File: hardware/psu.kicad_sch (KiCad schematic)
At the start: 14 parts, among them Q501 MMBT5551, U501 MAX15062AATA+T

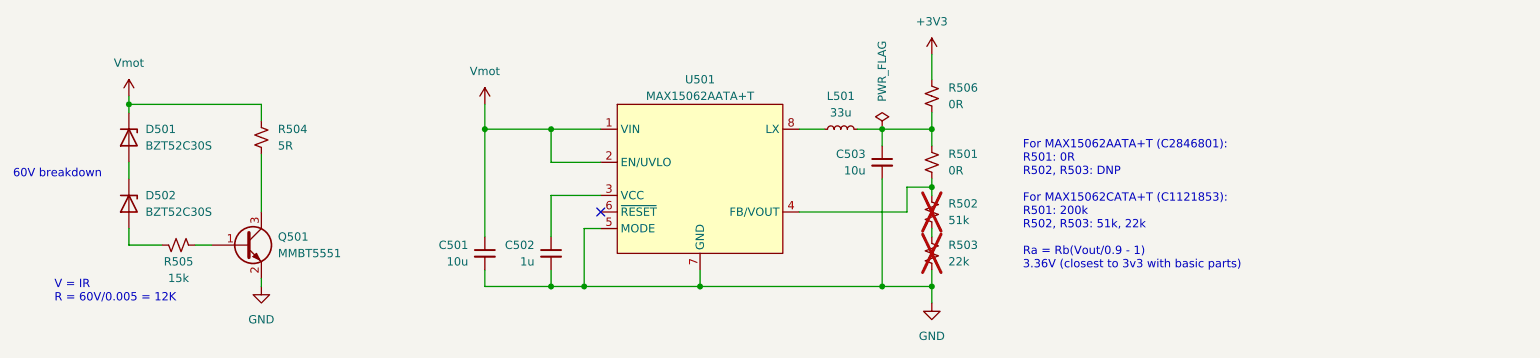
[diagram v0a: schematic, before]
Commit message: fix erc failures
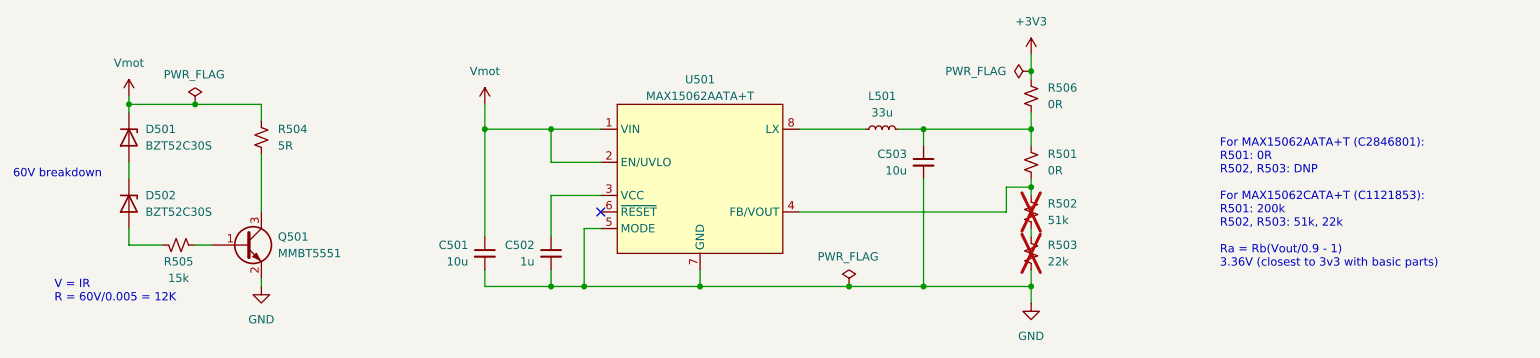
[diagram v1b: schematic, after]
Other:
- moved on the sheet: C503, L501, R501, R502, R503, R506

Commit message: Update BOM field LCSC ID
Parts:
- C501, C503: LCSC ID (none) -> C440198; LCSC Part C440198 -> (none)
- C502: LCSC ID (none) -> C52923; LCSC Part C52923 -> (none)
- D501, D502: LCSC ID (none) -> C22622; LCSC Part C22622 -> (none)
- L501: LCSC ID (none) -> C602034; LCSC Part C602034 -> (none)
- Q501: LCSC ID (none) -> C2145; LCSC Part C2145 -> (none)
- R501: LCSC ID (none) -> C17168; LCSC Part C17168 -> (none)
- R502: LCSC ID (none) -> C25794; LCSC Part C25794 -> (none)
- R503: LCSC ID (none) -> C25768; LCSC Part C25768 -> (none)
- R504: LCSC ID (none) -> C22936; LCSC Part C22936 -> (none)
- R505: LCSC ID (none) -> C25756; LCSC Part C25756 -> (none)
- R506: LCSC ID (none) -> C21189; LCSC Part C21189 -> (none)
- U501: LCSC ID (none) -> C2846801; LCSC Part C2846801 -> (none)
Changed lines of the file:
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@@
 			)
 		)
-		(property "LCSC Part" "C2145"
+		(property "LCSC ID" "C2145"
 			(at 76.2 92.71 0)
 			(effects
@@
 			)
 		)
-		(property "LCSC Part" "C52923"
+		(property "LCSC ID" "C52923"
 			(at 123.19 93.98 0)
 			(effects
@@
 			)
 		)
-		(property "LCSC Part" "C25756"
+		(property "LCSC ID" "C25756"
 			(at 66.04 92.71 0)
 			(effects
@@
 			)
 		)
-		(property "LCSC Part" "C2846801"
-			(at 146.05 101.6 0)
+		(property "LCSC ID" "C2846801"
+			(at 146.05 87.63 0)
 			(effects
 				(font
@@
 			)
 		)
-		(property "LCSC Part" "C22622"
+		(property "LCSC ID" "C22622"
 			(at 58.42 86.36 0)
 			(effects
@@
 			)
 		)
-		(property "LCSC Part" "C25768"
+		(property "LCSC ID" "C25768"
 			(at 196.85 93.98 0)
 			(effects
@@
 			)
 		)
-		(property "LCSC Part" "C22622"
+		(property "LCSC ID" "C22622"
 			(at 58.42 76.2 0)
 			(effects
@@
 			)
 		)
-		(property "LCSC Part" "C22936"
+		(property "LCSC ID" "C22936"
 			(at 78.74 76.2 0)
 			(effects
@@
 			)
 		)
-		(property "LCSC Part" "C21189"
+		(property "LCSC ID" "C21189"
 			(at 196.85 69.85 0)
 			(effects
@@
 			)
 		)
-		(property "LCSC Part" "C602034"
+		(property "LCSC ID" "C602034"
 			(at 173.99 74.93 0)
 			(effects
@@
 			)
 		)
-		(property "LCSC Part" "C440198"
+		(property "LCSC ID" "C440198"
 			(at 113.03 93.98 0)
 			(effects
@@
 			)
 		)
-		(property "LCSC Part" "C25794"
+		(property "LCSC ID" "C25794"
 			(at 196.85 87.63 0)
 			(effects
@@
 			)
 		)
-		(property "LCSC Part" "C440198"
+		(property "LCSC ID" "C440198"
 			(at 180.34 80.01 0)
 			(effects
@@
 			)
 		)
-		(property "LCSC Part" "C17168"
+		(property "LCSC ID" "C17168"
 			(at 196.85 80.01 0)
 			(effects

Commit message: fix BOM to use basic parts again
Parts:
- D501, D502: LCSC ID C22622 -> C19077418
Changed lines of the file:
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@@
 			)
 		)
-		(property "LCSC ID" "C22622"
+		(property "LCSC ID" "C19077418"
 			(at 58.42 86.36 0)
 			(effects
@@
 			)
 		)
-		(property "LCSC ID" "C22622"
+		(property "LCSC ID" "C19077418"
 			(at 58.42 76.2 0)
 			(effects

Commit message: add hybrid board outline
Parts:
- U501: footprint easyeda2kicad:TDFN-8_L2.0-W2.0-P0.50-BL -> Package_DFN_QFN:TDFN-8-1EP_2x2mm_P0.5mm_EP0.8x1.2mm
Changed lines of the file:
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@@
 			)
 		)
-		(property "Footprint" "easyeda2kicad:TDFN-8_L2.0-W2.0-P0.50-BL"
+		(property "Footprint" "Package_DFN_QFN:TDFN-8-1EP_2x2mm_P0.5mm_EP0.8x1.2mm"
 			(at 146.05 99.06 0)
 			(effects

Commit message: clean erc drc, pack sym, footprints into standalone lib
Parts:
- C501, C503: footprint Capacitor_SMD:C_0805_2012Metric -> lemon-pepper-footprints:C_0805_2012Metric; symbol Device:C_Small -> lemon-pepper-symbols:C_Small
- C502: footprint Capacitor_SMD:C_0402_1005Metric -> lemon-pepper-footprints:C_0402_1005Metric; symbol Device:C_Small -> lemon-pepper-symbols:C_Small
- D501, D502: footprint Diode_SMD:D_SOD-323 -> lemon-pepper-footprints:D_SOD-323; symbol Device:D_Zener -> lemon-pepper-symbols:D_Zener
- L501: footprint easyeda2kicad:IND-SMD_L4.0-W4.0 -> lemon-pepper-footprints:IND-SMD_L4.0-W4.0; symbol Device:L_Small -> lemon-pepper-symbols:L_Small
- Q501: footprint Package_TO_SOT_SMD:SOT-23 -> lemon-pepper-footprints:SOT-23; symbol Transistor_BJT:MMBT5551L -> lemon-pepper-symbols:MMBT5551L
- R501, R505: footprint Resistor_SMD:R_0402_1005Metric -> lemon-pepper-footprints:R_0402_1005Metric; symbol Device:R_Small_US -> lemon-pepper-symbols:R_Small_US
- R502, R503: symbol Device:R_Small_US -> lemon-pepper-symbols:R_Small_US
- R504, R506: footprint Resistor_SMD:R_0603_1608Metric -> lemon-pepper-footprints:R_0603_1608Metric; symbol Device:R_Small_US -> lemon-pepper-symbols:R_Small_US
- U501: footprint Package_DFN_QFN:TDFN-8-1EP_2x2mm_P0.5mm_EP0.8x1.2mm -> lemon-pepper-footprints:TDFN-8-1EP_2x2mm_P0.5mm_EP0.8x1.2mm; symbol easyeda2kicad:MAX15062CATA+T -> lemon-pepper-symbols:MAX15062CATA+T
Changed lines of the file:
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@@
 	)
 	(symbol
-		(lib_id "matei:Vmot")
+		(lib_id "power:+24V")
 		(at 113.03 71.12 0)
 		(unit 1)
@@
 			)
 		)
-		(property "Description" ""
+		(property "Description" "Power symbol creates a global label with name \"+24V\""
 			(at 113.03 71.12 0)
 			(effects
@@
 			)
 		)
-		(property "Description" ""
+		(property "Description" "Power symbol creates a global label with name \"GND\" , ground"
 			(at 196.85 101.6 0)
 			(effects
@@
 	)
 	(symbol
-		(lib_id "Transistor_BJT:MMBT5551L")
+		(lib_id "lemon-pepper-symbols:MMBT5551L")
 		(at 76.2 92.71 0)
 		(unit 1)
@@
 			)
 		)
-		(property "Footprint" "Package_TO_SOT_SMD:SOT-23"
+		(property "Footprint" "lemon-pepper-footprints:SOT-23"
 			(at 81.28 94.615 0)
 			(effects
@@
 			)
 		)
-		(property "Description" ""
+		(property "Description" "0.6A Ic, 160V Vce, NPN Transistor, SOT-23"
 			(at 76.2 92.71 0)
 			(effects
@@
 	)
 	(symbol
-		(lib_id "Device:C_Small")
+		(lib_id "lemon-pepper-symbols:C_Small")
 		(at 123.19 93.98 0)
 		(unit 1)
@@
 			)
 		)
-		(property "Footprint" "Capacitor_SMD:C_0402_1005Metric"
+		(property "Footprint" "lemon-pepper-footprints:C_0402_1005Metric"
 			(at 123.19 93.98 0)
 			(effects
@@
 			)
 		)
-		(property "Description" ""
+		(property "Description" "Unpolarized capacitor, small symbol"
 			(at 123.19 93.98 0)
 			(effects
@@
 	)
 	(symbol
-		(lib_id "Device:R_Small_US")
+		(lib_id "lemon-pepper-symbols:R_Small_US")
 		(at 66.04 92.71 90)
 		(mirror x)
@@
 			)
 		)
-		(property "Footprint" "Resistor_SMD:R_0402_1005Metric"
+		(property "Footprint" "lemon-pepper-footprints:R_0402_1005Metric"
 			(at 66.04 92.71 0)
 			(effects
@@
 			)
 		)
-		(property "Description" ""
+		(property "Description" "Resistor, small US symbol"
 			(at 66.04 92.71 0)
 			(effects
@@
 	)
 	(symbol
-		(lib_id "easyeda2kicad:MAX15062CATA+T")
+		(lib_id "lemon-pepper-symbols:MAX15062CATA+T")
 		(at 146.05 87.63 0)
 		(unit 1)
@@
 			)
 		)
-		(property "Footprint" "Package_DFN_QFN:TDFN-8-1EP_2x2mm_P0.5mm_EP0.8x1.2mm"
+		(property "Footprint" "lemon-pepper-footprints:TDFN-8-1EP_2x2mm_P0.5mm_EP0.8x1.2mm"
 			(at 146.05 99.06 0)
 			(effects
@@
 	)
 	(symbol
-		(lib_id "Device:D_Zener")
+		(lib_id "lemon-pepper-symbols:D_Zener")
 		(at 58.42 86.36 270)
 		(unit 1)
@@
 			)
 		)
-		(property "Footprint" "Diode_SMD:D_SOD-323"
+		(property "Footprint" "lemon-pepper-footprints:D_SOD-323"
 			(at 58.42 86.36 0)
 			(effects
@@
 			)
 		)
-		(property "Description" ""
+		(property "Description" "Zener diode"
 			(at 58.42 86.36 0)
 			(effects
@@
 	)
 	(symbol
-		(lib_id "Device:R_Small_US")
+		(lib_id "lemon-pepper-symbols:R_Small_US")
 		(at 196.85 93.98 0)
 		(unit 1)
@@
 			)
 		)
-		(property "Description" ""
+		(property "Description" "Resistor, small US symbol"
 			(at 196.85 93.98 0)
 			(effects
@@
 	)
 	(symbol
-		(lib_id "Device:D_Zener")
+		(lib_id "lemon-pepper-symbols:D_Zener")
 		(at 58.42 76.2 270)
 		(unit 1)
@@
 			)
 		)
-		(property "Footprint" "Diode_SMD:D_SOD-323"
+		(property "Footprint" "lemon-pepper-footprints:D_SOD-323"
 			(at 58.42 76.2 0)
 			(effects
@@
 			)
 		)
-		(property "Description" ""
+		(property "Description" "Zener diode"
 			(at 58.42 76.2 0)
 			(effects
@@
 	)
 	(symbol
-		(lib_id "Device:R_Small_US")
+		(lib_id "lemon-pepper-symbols:R_Small_US")
 		(at 78.74 76.2 0)
 		(unit 1)
@@
 			)
 		)
-		(property "Footprint" "Resistor_SMD:R_0603_1608Metric"
+		(property "Footprint" "lemon-pepper-footprints:R_0603_1608Metric"
 			(at 78.74 76.2 0)
 			(effects
@@
 			)
 		)
-		(property "Description" ""
+		(property "Description" "Resistor, small US symbol"
 			(at 78.74 76.2 0)
 			(effects
@@
 			)
 		)
-		(property "Description" ""
+		(property "Description" "Power symbol creates a global label with name \"GND\" , ground"
 			(at 78.74 99.06 0)
 			(effects
@@
 			)
 		)
-		(property "Description" ""
+		(property "Description" "Power symbol creates a global label with name \"+3V3\""
 			(at 196.85 63.5 0)
 			(effects
@@
 	)
 	(symbol
-		(lib_id "Device:R_Small_US")
+		(lib_id "lemon-pepper-symbols:R_Small_US")
 		(at 196.85 69.85 0)
 		(unit 1)
@@
 			)
 		)
-		(property "Footprint" "Resistor_SMD:R_0603_1608Metric"
+		(property "Footprint" "lemon-pepper-footprints:R_0603_1608Metric"
 			(at 196.85 69.85 0)
 			(effects
@@
 			)
 		)
-		(property "Description" ""
+		(property "Description" "Resistor, small US symbol"
 			(at 196.85 69.85 0)
 			(effects
@@
 	)
 	(symbol
-		(lib_id "Device:L_Small")
+		(lib_id "lemon-pepper-symbols:L_Small")
 		(at 173.99 74.93 90)
 		(unit 1)
@@
 			)
 		)
-		(property "Footprint" "easyeda2kicad:IND-SMD_L4.0-W4.0"
+		(property "Footprint" "lemon-pepper-footprints:IND-SMD_L4.0-W4.0"
 			(at 173.99 74.93 0)
 			(effects
@@
 			)
 		)
-		(property "Description" ""
+		(property "Description" "Inductor, small symbol"
 			(at 173.99 74.93 0)
 			(effects
@@
 	)
 	(symbol
-		(lib_id "matei:Vmot")
+		(lib_id "power:+24V")
 		(at 58.42 69.85 0)
 		(unit 1)
@@
 			)
 		)
-		(property "Description" ""
+		(property "Description" "Power symbol creates a global label with name \"+24V\""
 			(at 58.42 69.85 0)
 			(effects
@@
 	)
 	(symbol
-		(lib_id "Device:C_Small")
+		(lib_id "lemon-pepper-symbols:C_Small")
 		(at 113.03 93.98 0)
 		(unit 1)
@@
 			)
 		)
-		(property "Footprint" "Capacitor_SMD:C_0805_2012Metric"
+		(property "Footprint" "lemon-pepper-footprints:C_0805_2012Metric"
 			(at 113.03 93.98 0)
 			(effects
@@
 			)
 		)
-		(property "Description" ""
+		(property "Description" "Unpolarized capacitor, small symbol"
 			(at 113.03 93.98 0)
 			(effects
@@
 	)
 	(symbol
-		(lib_id "Device:R_Small_US")
+		(lib_id "lemon-pepper-symbols:R_Small_US")
 		(at 196.85 87.63 0)
 		(unit 1)
@@
 			)
 		)
-		(property "Description" ""
+		(property "Description" "Resistor, small US symbol"
 			(at 196.85 87.63 0)
 			(effects
@@
 	)
 	(symbol
-		(lib_id "Device:C_Small")
+		(lib_id "lemon-pepper-symbols:C_Small")
 		(at 180.34 80.01 0)
 		(unit 1)
@@
 			)
 		)
-		(property "Footprint" "Capacitor_SMD:C_0805_2012Metric"
+		(property "Footprint" "lemon-pepper-footprints:C_0805_2012Metric"
 			(at 180.34 80.01 0)
 			(effects
@@
 			)
 		)
-		(property "Description" ""
+		(property "Description" "Unpolarized capacitor, small symbol"
 			(at 180.34 80.01 0)
 			(effects
@@
 	)
 	(symbol
-		(lib_id "Device:R_Small_US")
+		(lib_id "lemon-pepper-symbols:R_Small_US")
 		(at 196.85 80.01 0)
 		(unit 1)
@@
 			)
 		)
-		(property "Footprint" "Resistor_SMD:R_0402_1005Metric"
+		(property "Footprint" "lemon-pepper-footprints:R_0402_1005Metric"
 			(at 196.85 80.01 0)
 			(effects
@@
 			)
 		)
-		(property "Description" ""
+		(property "Description" "Resistor, small US symbol"
 			(at 196.85 80.01 0)
 			(effects
